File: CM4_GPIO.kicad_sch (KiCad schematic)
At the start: 15 parts, among them J4 THD-20-R, U10 PUSB3FR4, U12 SI-51005-F, U2 74LVC1G07SE-7, U9 PUSB3FR4

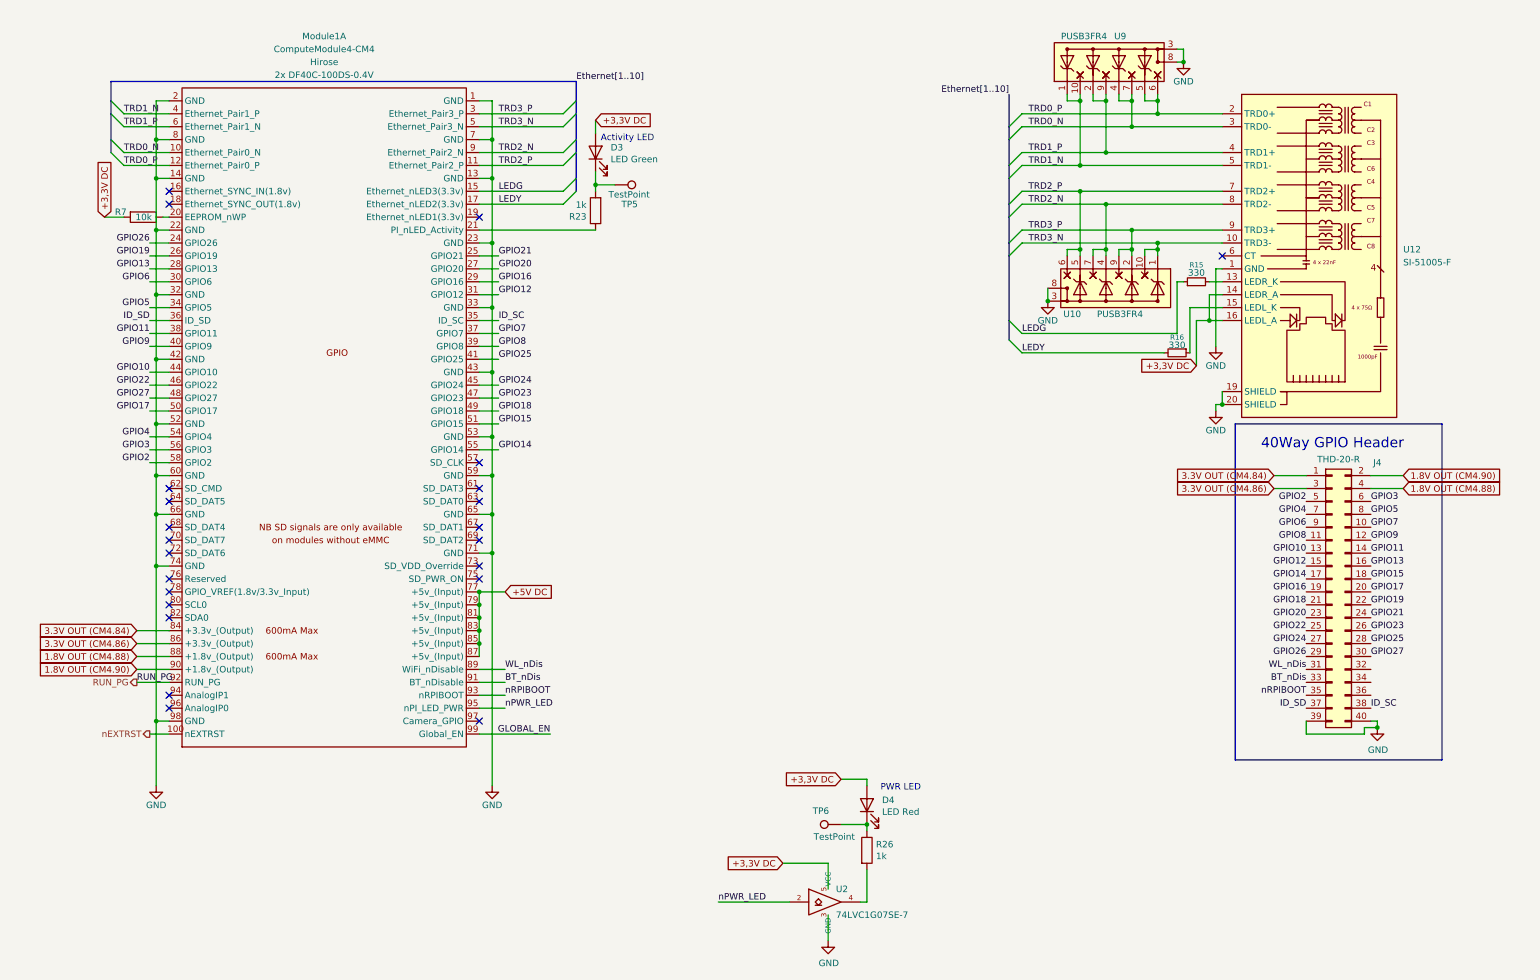
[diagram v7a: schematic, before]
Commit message: Redid the routing and fixed ERC warnings
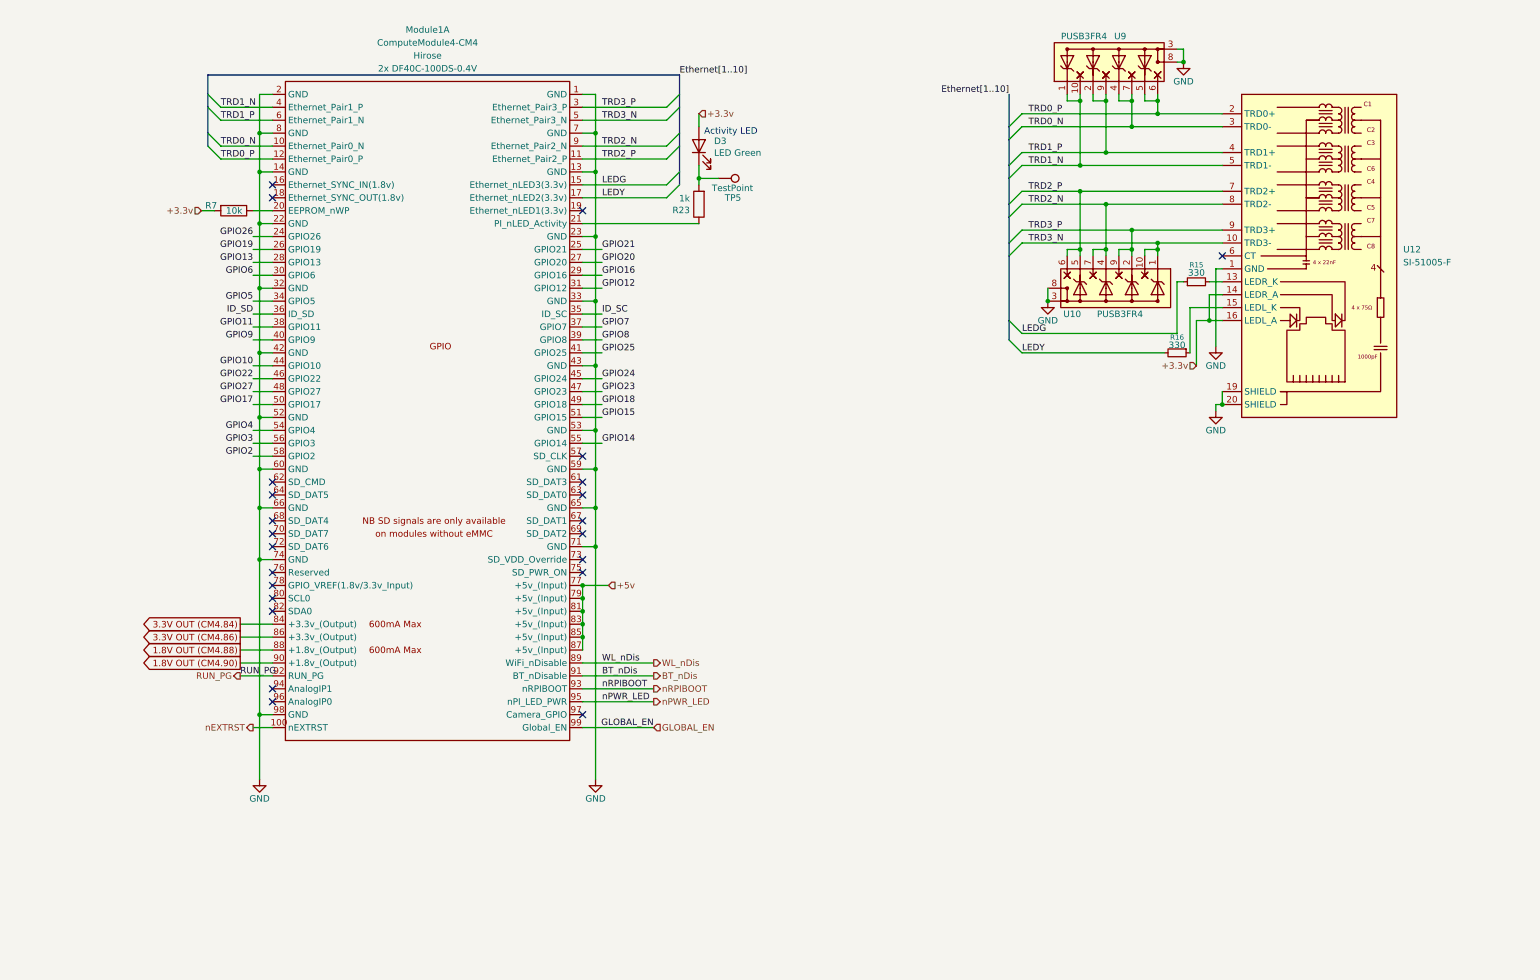
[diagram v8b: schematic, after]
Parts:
- removed D4: LED Red, LED_SMD:LED_0603_1608Metric, symbol Device:LED
- removed J4: THD-20-R, Connector_PinHeader_2.54mm:PinHeader_2x20_P2.54mm_Vertical, symbol Connector_Generic:Conn_02x20_Odd_Even
- removed R26: 1k, Resistor_SMD:R_0402_1005Metric_Pad0.72x0.64mm_HandSolder, symbol Device:R
- removed TP6: TestPoint, TestPoint:TestPoint_Pad_2.0x2.0mm, symbol Connector:TestPoint
- removed U2: 74LVC1G07SE-7, Package_TO_SOT_SMD:SOT-353_SC-70-5, symbol CM4IO:74LVC1G07_copy
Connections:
- net +3,3V DC renamed +3.3v
- net +5V DC renamed +5v
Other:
- note removed: "40Way GPIO Header"
- note removed: "PWR LED"
- moved on the sheet: D3, Module1A, R23, R7, TP5
